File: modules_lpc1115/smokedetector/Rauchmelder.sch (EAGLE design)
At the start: 70 parts, among them IC1 BD9G101, IC2 LPC1115, Q1 BC856, Q3 BCP52, Q4 ASFL, T1 BC847C

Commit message: [RM] - removed voltage divider again, added status LEDs, ...
- after a long discussion: we should use nowhere the voltage divider!
- status LEDs will help to identify problems when building the module
- optimized schematic
- added fiducials
- changed D1 to SMA footprint again
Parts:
- removed R23: 43k, rcl:R-EU_R1206
- removed R24: 340k, rcl:R-EU_R1206
- added LED2, LED3: (no value), led:LEDCHIPLED_1206
- added R2, R22: 1k, rcl:R-EU_R1206
- D1: device bt_diode:SCHOTTKY-DIODE-MBR130LSFT1 -> microbuilder:DIODESMA
- D2, D3, D4, D8: device diode:DIODE-MINIMELF -> microbuilder:DIODESOD-123
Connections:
- removed net EN: IC1.EN, R23.1, R24.2
- new net ARMINFO1: IC2.PIO3_3/RI/CT16B0_CAP0, R2.1
- new net ARMINFO2: IC2.PIO2_6/CT32B0_MAT1, R22.1
- new net N$3: LED2.A, R2.2
- new net N$5: LED3.A, R22.2
- net +3V3: now also LED2.C, LED3.C
- net EIB_DC: now also IC1.EN; no longer R24.1
- net GND: no longer R23.2
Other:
- note added: "3.8.4"
- note removed: ".... ich würde für den Enable Teiler 340k zu 43k vorschlagen. Der BD9G hat einen Ri von ca 500k am Pin und braucht am Pin >=2V um zu arbeiten. Der max Eingangsstrom liegt laut Datenblatt bei 11uA, mit den 380k Gesamt ist der Querstrom durch den Teiler ca 4-fach (47uA bei 18V), das sollte für ausreichend Genauigkeit bei Teilestreuung reichen"
- note removed: "3.0"
- note removed: "hora0815 via Slack:"
- moved on the sheet: C22, C7, FD1, FD2, FD3, FD4, LED1, R13, S1

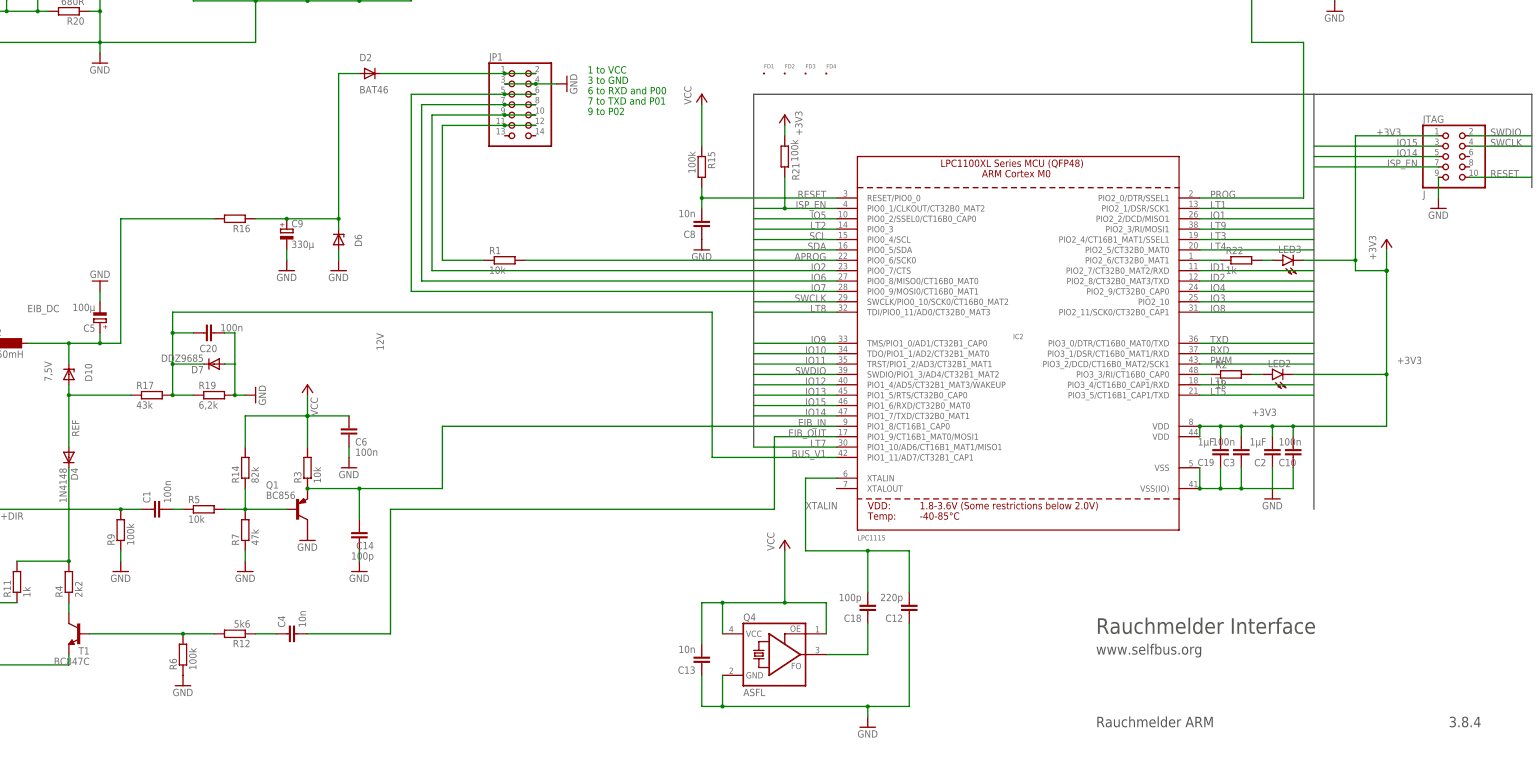
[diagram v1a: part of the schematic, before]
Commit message: [RM] Routed pwr suply switch / base detection
Merged olterions change with most recent verison
Routed addtional parts for base detection and pwr supply switch
Removed accidentially added v3.8.3
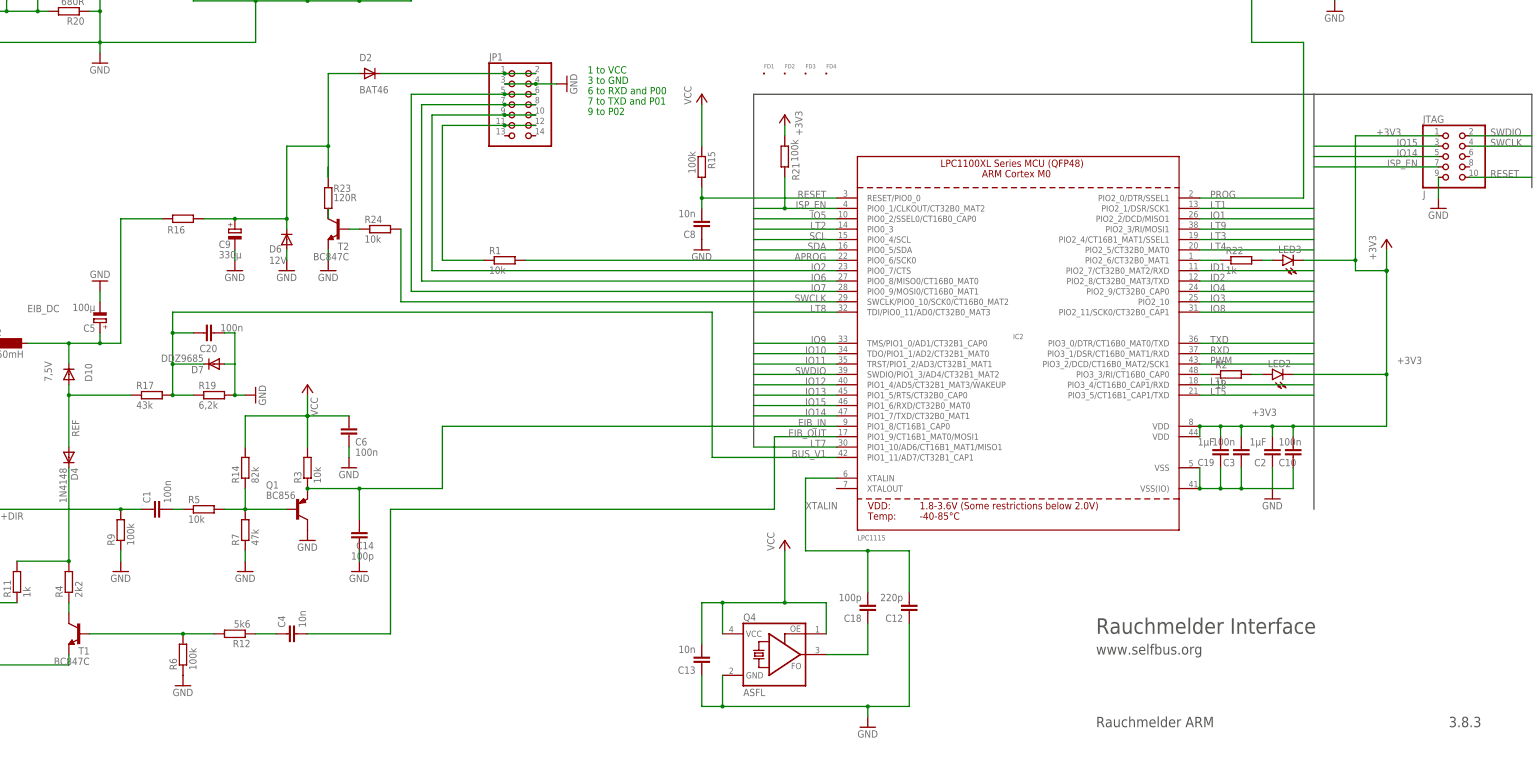
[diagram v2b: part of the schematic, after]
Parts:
- added R23: 120R, rcl:R-EU_R1206
- added R24: 10k, rcl:R-EU_R1206
- added T2: BC847C, transistor:BC847C
- D10, D6: device diode:ZPD -> microbuilder:DIODESOD-123
- D7: device diode:DIODE-MINIMELF -> microbuilder:DIODESOD-123
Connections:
- new net N$7: R23.2, T2.C
- new net N$8: R24.1, T2.B
- net GND: now also T2.E
- net LT1: now also R24.2
- net N$10: now also R23.1
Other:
- note added: "3.8.3"
- note removed: "3.8.4"
- moved on the sheet: C9, R16
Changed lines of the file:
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@@
 <part name="Q1" library="transistor-pnp" deviceset="BC856*" device="SMD" technology="ALT1" value="BC856"/>
 <part name="T1" library="transistor" deviceset="BC847C" device=""/>
-<part name="D10" library="diode" deviceset="ZPD" device="" value="7,5V"/>
-<part name="D6" library="diode" deviceset="ZPD" device="" value="12V"/>
+<part name="D10" library="microbuilder" deviceset="DIODE" device="SOD-123" value="7,5V"/>
+<part name="D6" library="microbuilder" deviceset="DIODE" device="SOD-123" value="12V"/>
 <part name="C5" library="rcl" library_urn="urn:adsk.eagle:library:334" deviceset="CPOL-EU" device="SANYO_SMD_C6" package3d_urn="urn:adsk.eagle:package:23465/1" value="100µ"/>
 <part name="C10" library="rcl" library_urn="urn:adsk.eagle:library:334" deviceset="C-EU" device="C1206" package3d_urn="urn:adsk.eagle:package:23618/2" value="100n"/>
@@
 <part name="R17" library="rcl" library_urn="urn:adsk.eagle:library:334" deviceset="R-EU_" device="R1206" package3d_urn="urn:adsk.eagle:package:23540/2" value="43k"/>
 <part name="R19" library="rcl" library_urn="urn:adsk.eagle:library:334" deviceset="R-EU_" device="R1206" package3d_urn="urn:adsk.eagle:package:23540/2" value="6,2k"/>
-<part name="D7" library="diode" deviceset="DIODE-" device="MINIMELF" value="DDZ9685">
+<part name="D7" library="microbuilder" deviceset="DIODE" device="SOD-123" value="DDZ9685">
 <attribute name="ALTERNATIVE" value="MMSZ4684T1G"/>
 </part>
@@
 <part name="LED3" library="led" library_urn="urn:adsk.eagle:library:259" deviceset="LED" device="CHIPLED_1206" package3d_urn="urn:adsk.eagle:package:15823/2"/>
 <part name="R22" library="rcl" library_urn="urn:adsk.eagle:library:334" deviceset="R-EU_" device="R1206" package3d_urn="urn:adsk.eagle:package:23540/2" value="1k"/>
+<part name="T2" library="transistor" deviceset="BC847C" device=""/>
+<part name="R23" library="rcl" deviceset="R-EU_" device="R1206" value="120R"/>
+<part name="R24" library="rcl" deviceset="R-EU_" device="R1206" value="10k"/>
+<part name="GND14" library="supply1" deviceset="GND" device=""/>
 </parts>
 <sheets>
@@
 <text x="317.5" y="27.94" size="2.54" layer="97">www.selfbus.org</text>
 <text x="317.5" y="10.16" size="2.54" layer="97">Rauchmelder ARM</text>
-<text x="403.86" y="10.16" size="2.54" layer="97">3.8.4</text>
+<text x="403.86" y="10.16" size="2.54" layer="97">3.8.3</text>
 <text x="193.04" y="165.1" size="1.778" layer="91">6 to RXD and P00</text>
 <text x="193.04" y="162.56" size="1.778" layer="91">7 to TXD and P01</text>
@@
 <attribute name="VALUE" x="110.49" y="36.322" size="1.778" layer="96" rot="R180"/>
 </instance>
-<instance part="GND19" gate="1" x="132.08" y="121.92" smashed="yes">
-<attribute name="VALUE" x="129.54" y="119.38" size="1.778" layer="96"/>
+<instance part="GND19" gate="1" x="119.38" y="121.92" smashed="yes">
+<attribute name="VALUE" x="116.84" y="119.38" size="1.778" layer="96"/>
 </instance>
 <instance part="GND11" gate="1" x="187.96" y="167.64" smashed="yes" rot="R90">
@@
 <attribute name="VALUE" x="218.44" y="162.56" size="1.778" layer="96" rot="R90"/>
 </instance>
-<instance part="R16" gate="G$1" x="106.68" y="134.62" smashed="yes" rot="R180">
-<attribute name="NAME" x="110.49" y="133.1214" size="1.778" layer="95" rot="R180"/>
-</instance>
-<instance part="C9" gate="G$1" x="119.38" y="132.08" smashed="yes">
-<attribute name="NAME" x="120.523" y="132.5626" size="1.778" layer="95"/>
-<attribute name="VALUE" x="120.523" y="127.4826" size="1.778" layer="96"/>
-</instance>
-<instance part="GND17" gate="1" x="119.38" y="121.92" smashed="yes">
-<attribute name="VALUE" x="116.84" y="119.38" size="1.778" layer="96"/>
+<instance part="R16" gate="G$1" x="93.98" y="134.62" smashed="yes" rot="R180">
+<attribute name="NAME" x="90.17" y="131.0386" size="1.778" layer="95"/>
+</instance>
+<instance part="C9" gate="G$1" x="106.68" y="132.08" smashed="yes">
+<attribute name="NAME" x="102.743" y="127.4826" size="1.778" layer="95"/>
+<attribute name="VALUE" x="102.743" y="124.9426" size="1.778" layer="96"/>
+</instance>
+<instance part="GND17" gate="1" x="106.68" y="121.92" smashed="yes">
+<attribute name="VALUE" x="104.14" y="119.38" size="1.778" layer="96"/>
 </instance>
 <instance part="D8" gate="G$1" x="27.94" y="104.14" smashed="yes">
@@
 <attribute name="VALUE" x="61.849" y="94.742" size="1.778" layer="96" rot="R90"/>
 </instance>
-<instance part="D6" gate="G$1" x="132.08" y="129.54" smashed="yes" rot="R90">
-<attribute name="NAME" x="137.795" y="127.762" size="1.778" layer="95" rot="R90"/>
-<attribute name="VALUE" x="143.129" y="102.362" size="1.778" layer="96" rot="R90"/>
+<instance part="D6" gate="G$1" x="119.38" y="129.54" smashed="yes" rot="R90">
+<attribute name="NAME" x="115.062" y="126.365" size="1.778" layer="95"/>
+<attribute name="VALUE" x="115.062" y="123.571" size="1.778" layer="96"/>
 </instance>
 <instance part="C5" gate="G$1" x="73.66" y="109.22" smashed="yes" rot="R180">
@@
 <attribute name="NAME" x="349.25" y="125.9586" size="1.778" layer="95"/>
 <attribute name="VALUE" x="349.25" y="121.158" size="1.778" layer="96"/>
+</instance>
+<instance part="T2" gate="G$1" x="132.08" y="132.08" smashed="yes" rot="MR0">
+<attribute name="NAME" x="134.62" y="127" size="1.778" layer="95" rot="MR0"/>
+<attribute name="VALUE" x="134.62" y="124.46" size="1.778" layer="96" rot="MR0"/>
+</instance>
+<instance part="R23" gate="G$1" x="129.54" y="139.7" smashed="yes" rot="R270">
+<attribute name="NAME" x="130.81" y="141.1986" size="1.778" layer="95"/>
+<attribute name="VALUE" x="130.81" y="138.938" size="1.778" layer="96"/>
+</instance>
+<instance part="R24" gate="G$1" x="142.24" y="132.08" smashed="yes">
+<attribute name="NAME" x="138.43" y="133.5786" size="1.778" layer="95"/>
+<attribute name="VALUE" x="138.43" y="128.778" size="1.778" layer="96"/>
+</instance>
+<instance part="GND14" gate="1" x="129.54" y="121.92" smashed="yes">
+<attribute name="VALUE" x="127" y="119.38" size="1.778" layer="96"/>
 </instance>
 </instances>
@@
 </segment>
 <segment>
-<wire x1="132.08" y1="127" x2="132.08" y2="124.46" width="0.1524" layer="91"/>
+<wire x1="119.38" y1="127" x2="119.38" y2="124.46" width="0.1524" layer="91"/>
 <pinref part="GND19" gate="1" pin="GND"/>
 <pinref part="D6" gate="G$1" pin="A"/>
@@
 <pinref part="C9" gate="G$1" pin="-"/>
 <pinref part="GND17" gate="1" pin="GND"/>
-<wire x1="119.38" y1="124.46" x2="119.38" y2="127" width="0.1524" layer="91"/>
+<wire x1="106.68" y1="124.46" x2="106.68" y2="127" width="0.1524" layer="91"/>
 </segment>
 <segment>
@@
 <junction x="137.16" y="187.96"/>
 </segment>
+<segment>
+<pinref part="T2" gate="G$1" pin="E"/>
+<pinref part="GND14" gate="1" pin="GND"/>
+<wire x1="129.54" y1="124.46" x2="129.54" y2="127" width="0.1524" layer="91"/>
+</segment>
 </net>
 <net name="N$2" class="0">
@@
 <net name="N$10" class="0">
 <segment>
-<wire x1="132.08" y1="134.62" x2="132.08" y2="170.18" width="0.1524" layer="91"/>
-<wire x1="132.08" y1="170.18" x2="137.16" y2="170.18" width="0.1524" layer="91"/>
-<wire x1="132.08" y1="132.08" x2="132.08" y2="134.62" width="0.1524" layer="91"/>
-<wire x1="111.76" y1="134.62" x2="119.38" y2="134.62" width="0.1524" layer="91"/>
-<wire x1="119.38" y1="134.62" x2="132.08" y2="134.62" width="0.1524" layer="91"/>
-<junction x="132.08" y="134.62"/>
+<wire x1="119.38" y1="132.08" x2="119.38" y2="134.62" width="0.1524" layer="91"/>
+<wire x1="99.06" y1="134.62" x2="106.68" y2="134.62" width="0.1524" layer="91"/>
+<wire x1="106.68" y1="134.62" x2="119.38" y2="134.62" width="0.1524" layer="91"/>
 <junction x="119.38" y="134.62"/>
+<junction x="106.68" y="134.62"/>
 <pinref part="R16" gate="G$1" pin="1"/>
 <pinref part="C9" gate="G$1" pin="+"/>
 <pinref part="D2" gate="G$1" pin="A"/>
 <pinref part="D6" gate="G$1" pin="C"/>
+<wire x1="119.38" y1="134.62" x2="119.38" y2="152.4" width="0.1524" layer="91"/>
+<wire x1="129.54" y1="170.18" x2="137.16" y2="170.18" width="0.1524" layer="91"/>
+<wire x1="129.54" y1="147.32" x2="129.54" y2="144.78" width="0.1524" layer="91"/>
+<wire x1="129.54" y1="144.78" x2="129.54" y2="152.4" width="0.1524" layer="91"/>
+<pinref part="R23" gate="G$1" pin="1"/>
+<wire x1="119.38" y1="152.4" x2="129.54" y2="152.4" width="0.1524" layer="91"/>
+<wire x1="129.54" y1="152.4" x2="129.54" y2="170.18" width="0.1524" layer="91"/>
+<junction x="129.54" y="152.4"/>
 </segment>
 </net>
@@
 <label x="345.44" y="137.16" size="1.778" layer="95"/>
 </segment>
+<segment>
+<pinref part="R24" gate="G$1" pin="2"/>
+<wire x1="147.32" y1="132.08" x2="147.32" y2="114.3" width="0.1524" layer="91"/>
+<wire x1="147.32" y1="114.3" x2="233.68" y2="114.3" width="0.1524" layer="91"/>
+</segment>
 </net>
 <net name="LT2" class="0">
@@
 <wire x1="66.04" y1="104.14" x2="73.66" y2="104.14" width="0.1524" layer="91"/>
 <wire x1="73.66" y1="104.14" x2="78.74" y2="104.14" width="0.1524" layer="91"/>
-<wire x1="101.6" y1="134.62" x2="78.74" y2="134.62" width="0.1524" layer="91"/>
+<wire x1="88.9" y1="134.62" x2="78.74" y2="134.62" width="0.1524" layer="91"/>
 <pinref part="L2" gate="G$1" pin="2"/>
 <pinref part="R16" gate="G$1" pin="2"/>
@@
 </segment>
 </net>
+<net name="N$7" class="0">
+<segment>
+<pinref part="R23" gate="G$1" pin="2"/>
+<pinref part="T2" gate="G$1" pin="C"/>
+<wire x1="129.54" y1="137.16" x2="129.54" y2="134.62" width="0.1524" layer="91"/>
+</segment>
+</net>
+<net name="N$8" class="0">
+<segment>
+<pinref part="T2" gate="G$1" pin="B"/>
+<pinref part="R24" gate="G$1" pin="1"/>
+<wire x1="137.16" y1="132.08" x2="134.62" y2="132.08" width="0.1524" layer="91"/>
+</segment>
+</net>
